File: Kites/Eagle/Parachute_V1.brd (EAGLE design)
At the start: 172.7 x 106.4 mm, 24 parts, among them Q1 MOSFET-NCH, Q2 MOSFET-NCH, U1 ITSYBITSY_5V, X1 MSTBA8

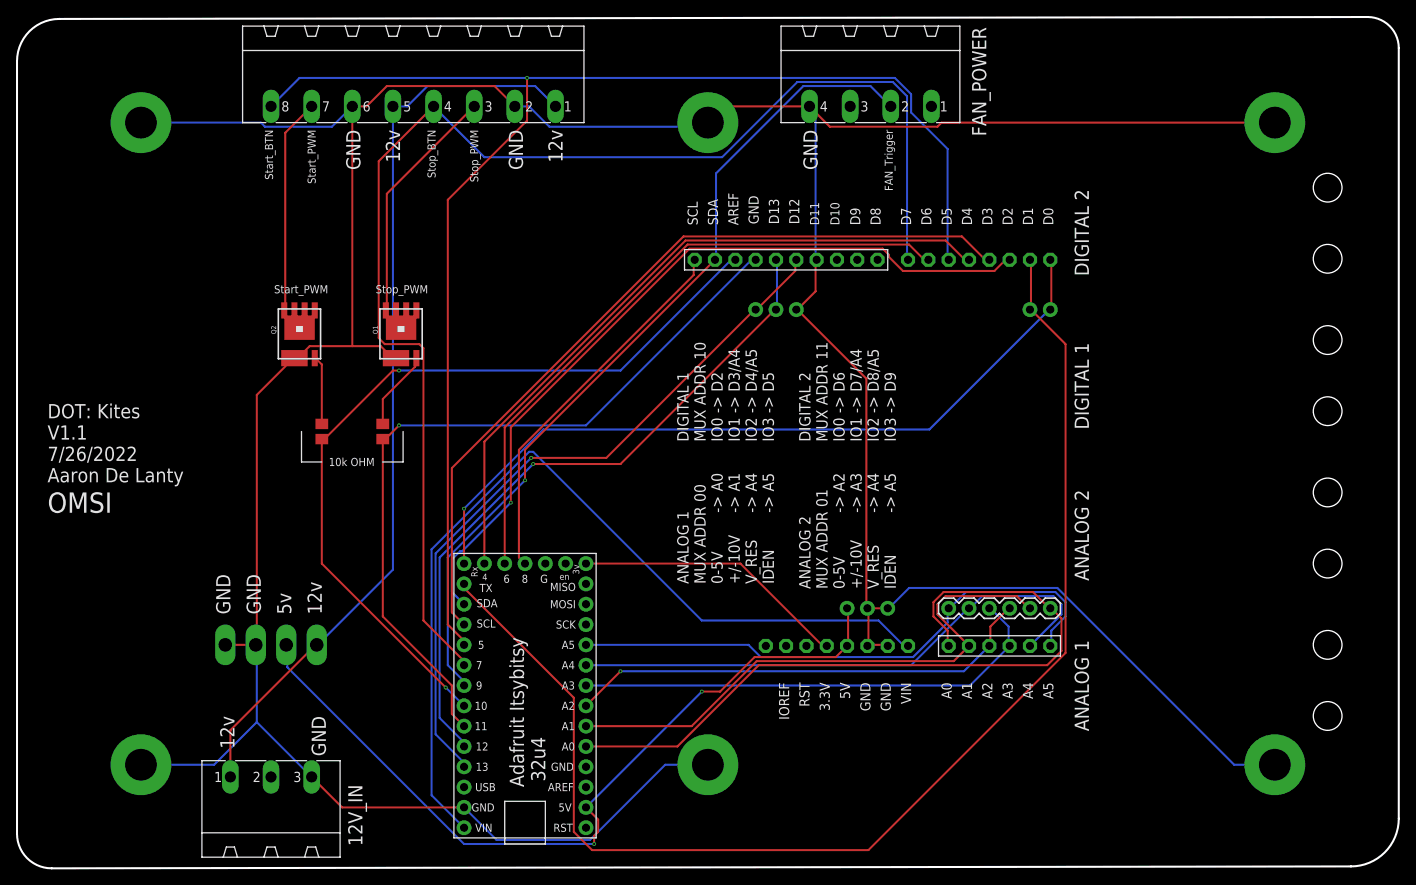
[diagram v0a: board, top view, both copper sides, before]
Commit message: Fixed pinout on board causing StopbtnPWN to ground Updated code to have proper breathing animation for each button
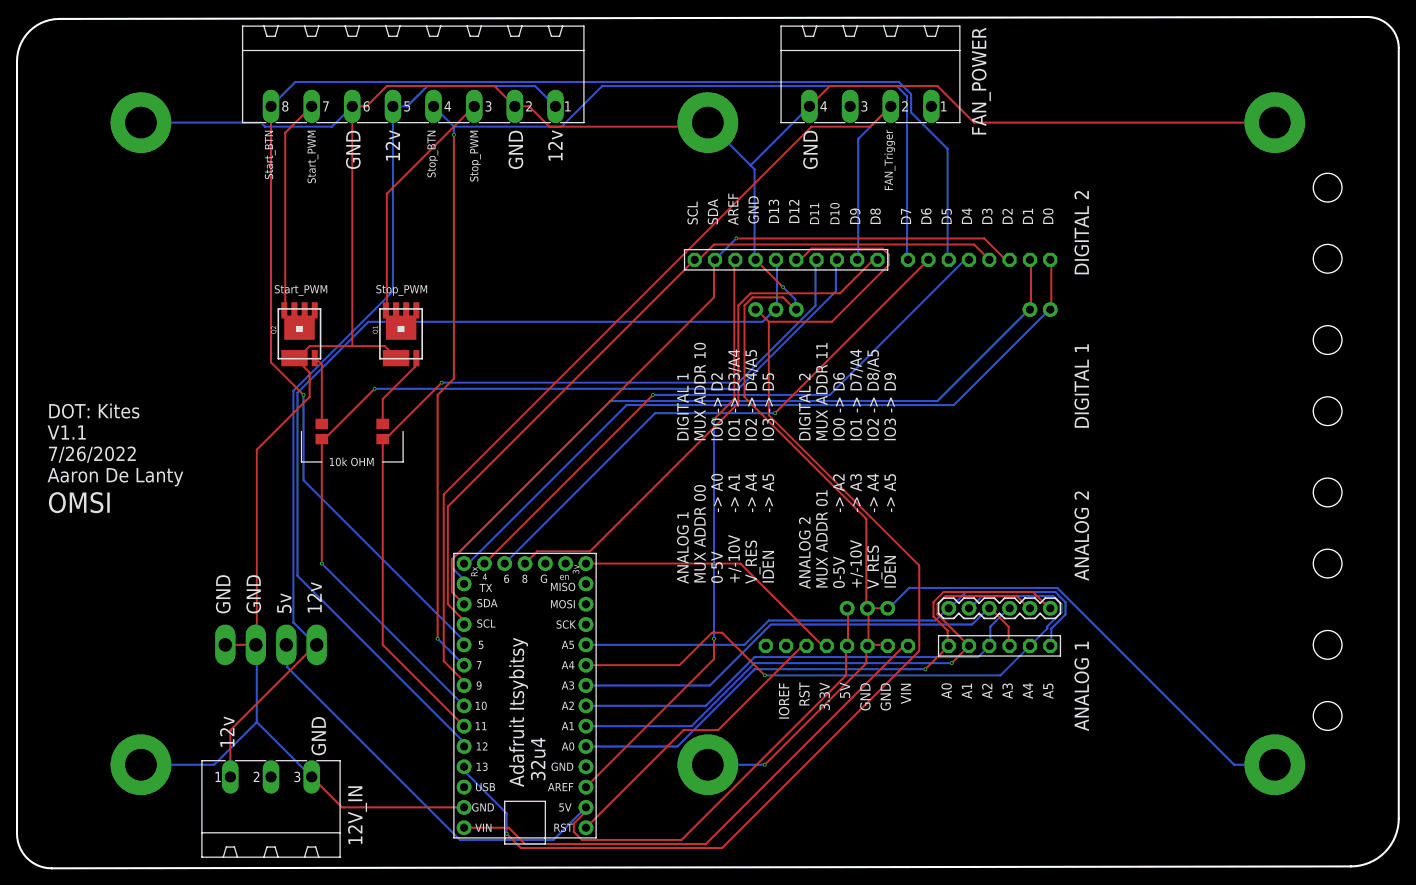
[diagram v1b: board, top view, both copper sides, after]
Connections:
- new net N$23: JP2.6, U1.RES
- new net N$6: U$1.8, U1.AREF
- net GND: now also U$1.7; no longer U$1.4
- net N$16: now also U$1.9
- net N$17: now also U$1.10
- net N$27: now also U$1.2; no longer U$1.9
- net N$28: now also U$1.3; no longer U$1.8
- net N$29: now also U$1.4; no longer U$1.7
- net N$4: now also U$1.1; no longer U$1.10
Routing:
- net N$6: track 0.00 -> 73.6 mm, vias 0 -> 2
- net N$18: track 89.2 -> 156.0 mm
- net N$5: track 160.4 -> 95.3 mm
- net N$31: track 111.1 -> 66.6 mm
- net N$15: track 86.2 -> 123.4 mm, vias 1 -> 0
- net N$23: track 0.00 -> 37.0 mm
- net N$8: track 92.6 -> 72.8 mm, vias 0 -> 1
- net N$4: track 47.4 -> 66.9 mm
- net N$27: track 106.2 -> 121.8 mm, vias 1 -> 0
- net N$28: track 101.9 -> 116.8 mm
- net N$21: track 166.6 -> 152.9 mm, vias 0 -> 2
- net N$20: track 80.2 -> 68.7 mm, vias 0 -> 1
- net N$22: track 87.2 -> 76.3 mm, vias 0 -> 1
- net N$29: track 96.2 -> 107.1 mm
- net N$13: track 70.3 -> 80.4 mm, vias 0 -> 1
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
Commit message: Updated repository to match most recent revisions
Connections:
- removed net N$23: JP2.6, U1.RES
- net N$22: now also JP2.6, U1.RES
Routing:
- net N$22: track 76.3 -> 154.0 mm, vias 1 -> 2
- net N$23: track 37.0 -> 0.00 mm
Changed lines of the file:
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@@
 <wire x1="107.442" y1="77.216" x2="107.569" y2="77.343" width="0.254" layer="16"/>
 <via x="68.072" y="60.452" extent="1-16" drill="0.254"/>
+<contactref element="U1" pad="RES"/>
+<contactref element="JP2" pad="6"/>
+<wire x1="86.614" y1="28.956" x2="87.122" y2="28.956" width="0.254" layer="1"/>
+<wire x1="76.2" y1="18.542" x2="86.614" y2="28.956" width="0.254" layer="1"/>
+<wire x1="71.882" y1="18.542" x2="76.2" y2="18.542" width="0.254" layer="1"/>
+<wire x1="59.69" y1="6.35" x2="71.882" y2="18.542" width="0.254" layer="1"/>
+<wire x1="87.122" y1="28.956" x2="87.249" y2="29.083" width="0.254" layer="1"/>
+<wire x1="58.166" y1="6.35" x2="59.69" y2="6.35" width="0.254" layer="16"/>
+<wire x1="57.404" y1="5.588" x2="58.166" y2="6.35" width="0.254" layer="16"/>
+<wire x1="57.404" y1="28.956" x2="57.404" y2="5.588" width="0.254" layer="1"/>
+<wire x1="46.99" y1="39.37" x2="57.404" y2="28.956" width="0.254" layer="1"/>
+<via x="57.404" y="5.588" extent="1-16" drill="0.254"/>
 </signal>
 <signal name="N$27">
@@
 <via x="75.692" y="29.972" extent="1-16" drill="0.254"/>
 </signal>
-<signal name="N$23">
-<contactref element="U1" pad="RES"/>
-<contactref element="JP2" pad="6"/>
-<wire x1="86.614" y1="28.956" x2="87.122" y2="28.956" width="0.254" layer="1"/>
-<wire x1="76.2" y1="18.542" x2="86.614" y2="28.956" width="0.254" layer="1"/>
-<wire x1="71.882" y1="18.542" x2="76.2" y2="18.542" width="0.254" layer="1"/>
-<wire x1="59.69" y1="6.35" x2="71.882" y2="18.542" width="0.254" layer="1"/>
-<wire x1="87.122" y1="28.956" x2="87.249" y2="29.083" width="0.254" layer="1"/>
-</signal>
 </signals>
